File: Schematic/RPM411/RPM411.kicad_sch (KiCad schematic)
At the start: 75 parts, among them J1 Conn_02x08_Unknow, U1 STM32F100C8Tb8

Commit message: Updated Overlay with proper names
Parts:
- added R34: DNP, Resistor_SMD:R_0402_1005Metric, symbol Device:R
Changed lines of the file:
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@@
+    (pin "2")
+  )
+  (symbol (lib_id "Device:R") (at 58.42 128.905 0) (unit 1)
+    (in_bom yes) (on_board yes) (fields_autoplaced)
+    (property "Reference" "R34" (id 0) (at 60.96 127.6349 0)
+      (effects (font (size 1.27 1.27)) (justify left))
+    )
+    (property "Value" "DNP" (id 1) (at 60.96 130.1749 0)
+      (effects (font (size 1.27 1.27)) (justify left))
+    )
+    (property "Footprint" "Resistor_SMD:R_0402_1005Metric" (id 2) (at 56.642 128.905 90)
+      (effects (font (size 1.27 1.27)) hide)
+    )
+    (property "Datasheet" "~" (id 3) (at 58.42 128.905 0)
+      (effects (font (size 1.27 1.27)) hide)
+    )
+    (pin "1")
     (pin "2")
   )
@@
       (reference "R33") (unit 1) (value "68R") (footprint "Resistor_SMD:R_0402_1005Metric")
     )
+    (path "/ce490511-0521-4d01-9983-ec2527fa23d6"
+      (reference "R34") (unit 1) (value "DNP") (footprint "Resistor_SMD:R_0402_1005Metric")
+    )
     (path "/118ff4b8-eefd-44e5-bf4d-827641d0eb1a"

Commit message: added pressure cap
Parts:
- added P1: P_Cap, RPM411:Pressure_Cap, symbol RPM411:C_Shield
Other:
- moved on the sheet: SH1
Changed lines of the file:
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@@
     (pin "2")
   )
-  (symbol (lib_id "Device:RFShield_OnePiece") (at 147.32 34.29 0) (unit 1)
-    (in_bom yes) (on_board yes) (fields_autoplaced)
-    (property "Reference" "SH1" (id 0) (at 152.4 36.83 0)
-      (effects (font (size 1.27 1.27)) (justify left))
-    )
-    (property "Value" "RFShield" (id 1) (at 152.4 39.37 0)
-      (effects (font (size 1.27 1.27)) (justify left))
-    )
-    (property "Footprint" "RPM411:RMP411_Shield" (id 2) (at 147.32 36.83 0)
-      (effects (font (size 1.27 1.27)) hide)
-    )
-    (property "Datasheet" "~" (id 3) (at 147.32 36.83 0)
+  (symbol (lib_id "Device:RFShield_OnePiece") (at 154.94 34.29 0) (unit 1)
+    (in_bom yes) (on_board yes) (fields_autoplaced)
+    (property "Reference" "SH1" (id 0) (at 160.02 36.83 0)
+      (effects (font (size 1.27 1.27)) (justify left))
+    )
+    (property "Value" "RFShield" (id 1) (at 160.02 39.37 0)
+      (effects (font (size 1.27 1.27)) (justify left))
+    )
+    (property "Footprint" "RPM411:RMP411_Shield" (id 2) (at 154.94 36.83 0)
+      (effects (font (size 1.27 1.27)) hide)
+    )
+    (property "Datasheet" "~" (id 3) (at 154.94 36.83 0)
       (effects (font (size 1.27 1.27)) hide)
     )
@@
     (pin "2")
   )
+  (symbol (lib_name "C_Shield_1") (lib_id "RPM411:C_Shield") (at 95.25 22.86 0) (unit 1)
+    (in_bom yes) (on_board yes) (fields_autoplaced)
+    (property "Reference" "P1" (id 0) (at 95.25 13.97 0))
+    (property "Value" "P_Cap" (id 1) (at 95.25 16.51 0))
+    (property "Footprint" "RPM411:Pressure_Cap" (id 2) (at 95.25 22.86 0)
+      (effects (font (size 1.27 1.27)) hide)
+    )
+    (property "Datasheet" "" (id 3) (at 95.25 22.86 0)
+      (effects (font (size 1.27 1.27)) hide)
+    )
+    (pin "1")
+    (pin "2")
+    (pin "SH")
+  )
   (symbol (lib_id "Device:R") (at 44.45 96.52 0) (unit 1)
     (in_bom yes) (on_board yes) (fields_autoplaced)
@@
       (reference "L4") (unit 1) (value "tbd") (footprint "Inductor_SMD:L_0402_1005Metric")
     )
+    (path "/8c0adcc2-e8a0-440b-aa06-db46eab446f7"
+      (reference "P1") (unit 1) (value "P_Cap") (footprint "RPM411:Pressure_Cap")
+    )
     (path "/254d263f-b4aa-4b21-bd5d-21e0f151fb34"

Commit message: identified ICs
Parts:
- added Q1: tbd (GDS), Package_TO_SOT_SMD:SOT-523, symbol Device:Q_PMOS_GDS
- added U2, U3, U4: TS5A9411, Package_TO_SOT_SMD:SOT-363_SC-70-6, symbol Analog_Switch:TS5A3159ADBVR
- added U5: 74LVC3G04, Package_SO:SSOP-8_3.95x5.21x3.27mm_P1.27mm, symbol 74xGxx:74LVC3G04
- added U6: 74LVC1G32, Package_TO_SOT_SMD:SOT-353_SC-70-5, symbol 74xGxx:74AHC1G32
- added U7: TLV70030DDC, Package_TO_SOT_SMD:SOT-23-5, symbol Regulator_Linear:TLV70030_SOT23-5
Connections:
- new net GND: U5.4 (GND), U5.4 (GND), U5.4 (GND), U6.3 (GND)
- new net VCC: U5.8 (VCC), U5.8 (VCC), U5.8 (VCC), U6.5 (VCC)

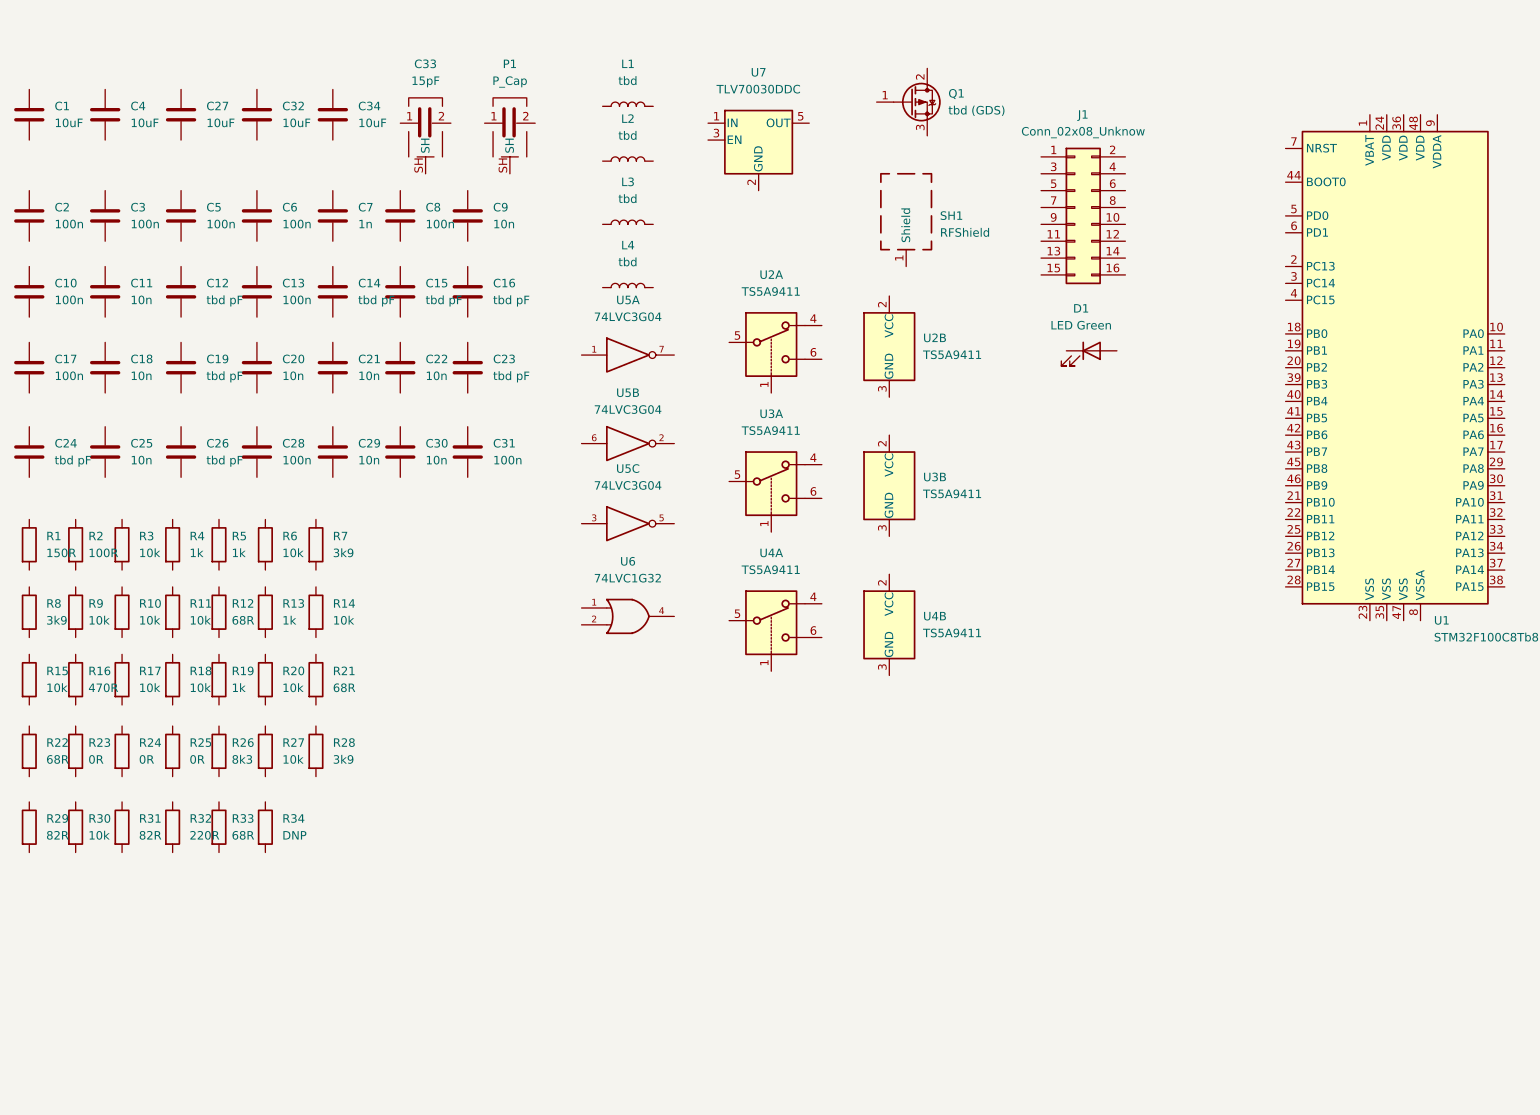
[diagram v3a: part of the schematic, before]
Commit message: added ground connections
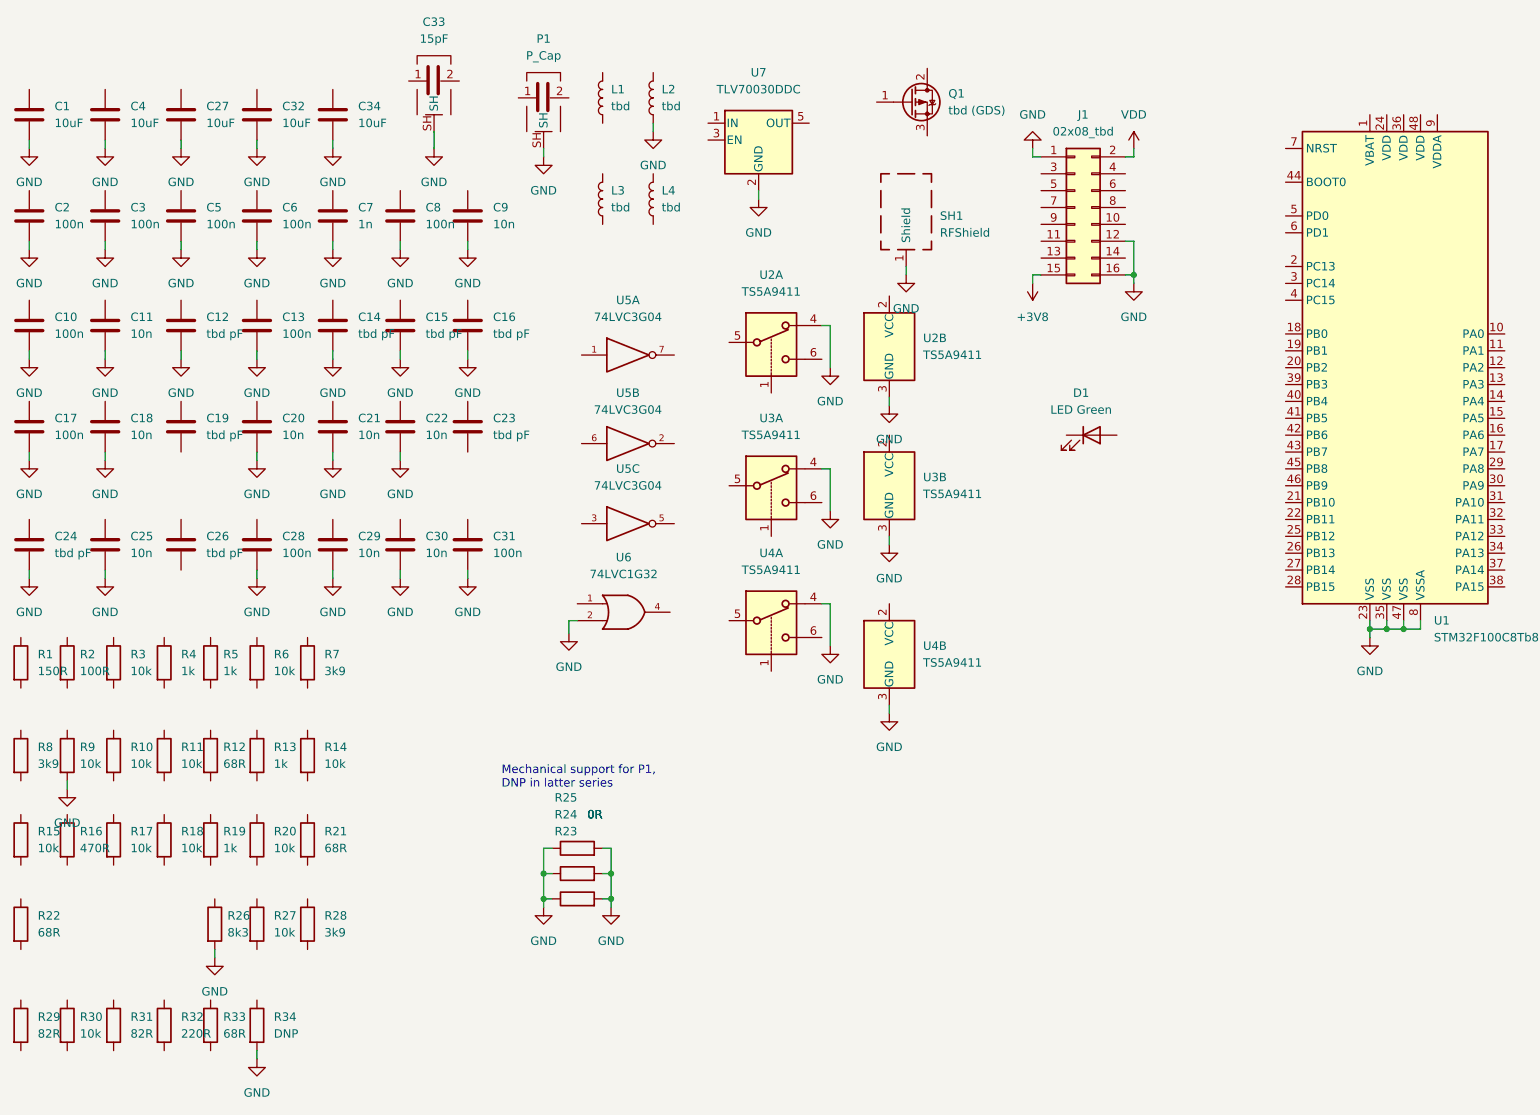
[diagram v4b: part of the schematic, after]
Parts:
- J1: value Conn_02x08_Unknow -> 02x08_tbd
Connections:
- net GND: now also C1.2, C10.2, C11.2, C12.2, C13.2, C14.2, C15.2, C16.2, C17.2, C18.2, C2.2, C20.2, C21.2, C22.2, C24.2, C25.2, C27.2, C28.2, C29.2, C3.2, C30.2, C31.2, C32.2, C33.SH, C34.2, C4.2, C5.2, C6.2, C7.2, C8.2, C9.2, J1.1 (Pin_1), J1.12 (Pin_12), J1.16 (Pin_16), L2.1, P1.SH, R23.1, R23.2, R24.1, R24.2, R25.1, R25.2, R26.2, R34.2, R9.2, SH1.1 (Shield), U1.23 (VSS), U1.35 (VSS), U1.47 (VSS), U1.8 (VSSA), U2.3 (GND), U2.4, U3.3 (GND), U3.4, U4.3 (GND), U4.4, U6.2, U7.2 (GND)
- net +3V8: now reaches J1.15 (Pin_15)
- net VDD: now reaches J1.2 (Pin_2)
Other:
- note added: "Mechanical support for P1, DNP in latter series"
- moved on the sheet: C10, C11, C12, C13, C14, C15, C16, C17, C18, C19, C20, C21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

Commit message: completed schematic
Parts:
- added TP1: Pin5, TestPoint:TestPoint_Pad_D1.0mm, symbol Connector:TestPoint
- added TP2: CS_E, TestPoint:TestPoint_Pad_D1.0mm, symbol Connector:TestPoint
- added TP3: CS_P, TestPoint:TestPoint_Pad_D1.0mm, symbol Connector:TestPoint
- added TP4: SDI, TestPoint:TestPoint_Pad_D1.0mm, symbol Connector:TestPoint
- J1: footprint (none) -> Connector_PinHeader_1.00mm:PinHeader_2x08_P1.00mm_Vertical
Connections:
- net +3V8: now also C1.1, C2.1, C31.1, C32.1, R1.2, U7.1 (IN), U7.3 (EN); no longer J1.15 (Pin_15)
- net GND: now also C12.1, C9.1, R9.1; no longer C12.2, C9.2, R9.2
- net VCC: now also C18.1, C20.1, C21.1, C22.1, C25.1, L4.1, Q1.2 (D), R10.2, U2.2 (VCC), U3.2 (VCC), U4.2 (VCC)
- net VDD: now also C10.1, C13.1, C17.1, C3.1, C34.1, C4.1, C5.1, C7.1, C8.1, L1.2, R16.1, R27.2, U1.1 (VBAT), U1.24 (VDD), U1.36 (VDD), U1.48 (VDD), U1.9 (VDDA); no longer J1.2 (Pin_2)
- net at R29.1: now also U5.2, U5.3
- net at R29.2: now also C23.1
- net Pullup: now reaches Q1.1 (G)
- net Pullup: now also C12.2, R15.1, R34.1
- net at Q1.3 (S): now also C19.1, C26.1, C33.2, P1.2, R32.2, U5.1
- net LED: now reaches C11.1
- net LED: now also D1.1 (K), L3.2
- net at C33.1: now also U4.5
- net VCCA_mon: now reaches R10.1
- net VCCA_mon: now also C9.2, R9.2, U1.18 (PB0)
- net at R12.1: now also U1.16 (PA6)
- net SPI_SDO: now reaches R12.2
- net SPI_SDO: now also J1.6 (Pin_6)
- net at U7.4 (NC): now also C30.1
- net at U7.5 (OUT): now also C27.1, C28.1, L4.2
- net at R22.1: now also U1.30 (PA9)
- net UART_TX: now reaches R22.2
- net UART_TX: now also J1.3 (Pin_3)
- net at U5.6: now also R31.2, U5.7
- net at R13.1: now also U1.15 (PA5)
- net SPI_SCK: now reaches R13.2
- net SPI_SCK: now also J1.4 (Pin_4)
- net at R32.1: now also R30.2, R33.2, U6.4
- net Switch_2: now reaches U3.1
- net Switch_2: now also C15.1, R18.1
- net at U3.6: now also C19.2, C23.2, R28.2, U2.6, U4.6, U5.5
- net at R5.1: now also U1.7 (NRST)
- net NRST: now reaches R5.2
- net NRST: now also C6.1, R2.1
- net at R1.1: now also J1.15 (Pin_15)
- net at R21.1: now also U1.34 (PA13)
- net SWDIO: now reaches R21.2
- net SWDIO: now also J1.11 (Pin_11), TP1.1
- net at R6.1: now also U1.10 (PA0), U1.20 (PB2)
- net CS_EEPROM: now reaches R6.2
- net CS_EEPROM: now also J1.10 (Pin_10), TP2.1
- net at U1.11 (PA1): now also R7.1
- net at U1.17 (PA7): now also R11.1
- net at U1.19 (PB1): now also R14.2
- net at U1.22 (PB11): now also L3.1
- net at U1.25 (PB12): now also R15.2
- net at U1.31 (PA10): now also R3.1
- net at U1.37 (PA14): now also R19.1
- net at U1.39 (PB3): now also R20.2
- net at U1.41 (PB5): now also R18.2
- net at U1.42 (PB6): now also R17.2
- net at U1.5 (PD0): now also R4.2
- net at U6.1: now also C24.1, R28.1, R30.1
- net at D1.2 (A): now also R16.2
- net SWCLK : now reaches R19.2
- net SWCLK : now also J1.9 (Pin_9)
- net Switch_3: now reaches R20.1
- net Switch_3: now also C16.1, U4.1
- net at R33.1: now also R8.2
- net VCCD_mon: now reaches C29.1
- net VCCD_mon: now also R14.1, R26.1, R27.1
- net Out: now reaches R8.1
- net Out: now also L2.2, R7.2
- net at J1.13 (Pin_13): now also R2.2
- net CS_Pressure: now reaches J1.14 (Pin_14)
- net CS_Pressure: now also R4.1, TP3.1
- net UART_RX: now reaches J1.5 (Pin_5)
- net UART_RX: now also R3.2
- net SPI_SDI: now reaches J1.8 (Pin_8)
- net SPI_SDI: now also R11.2, TP4.1
- net at C26.2: now also R31.1
- net Switch_1: now reaches R17.1
- net Switch_1: now also C14.1, U2.1
- net at P1.1: now also U2.5
- net at L1.1: now also J1.2 (Pin_2)
- no-connect marks 0 -> 21
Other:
- moved on the sheet: C1, C10, C11, C12, C13, C14, C15, C16, C17, C18, C19, C2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
